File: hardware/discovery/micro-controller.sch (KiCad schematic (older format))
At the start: 3 parts, among them U4 STM32F407VG

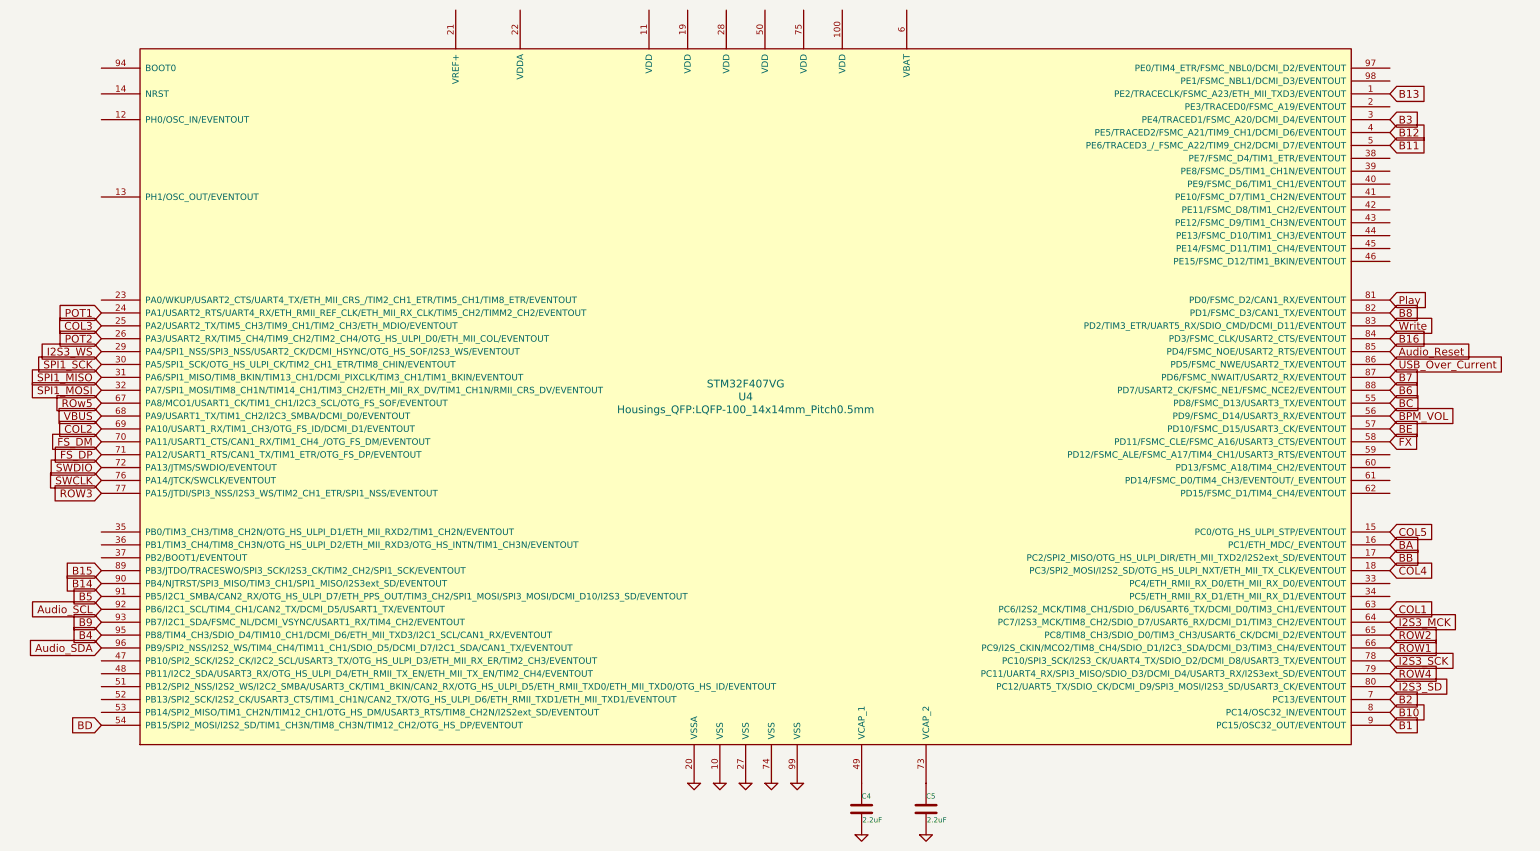
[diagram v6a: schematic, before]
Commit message: Discovery: Add audio DAC
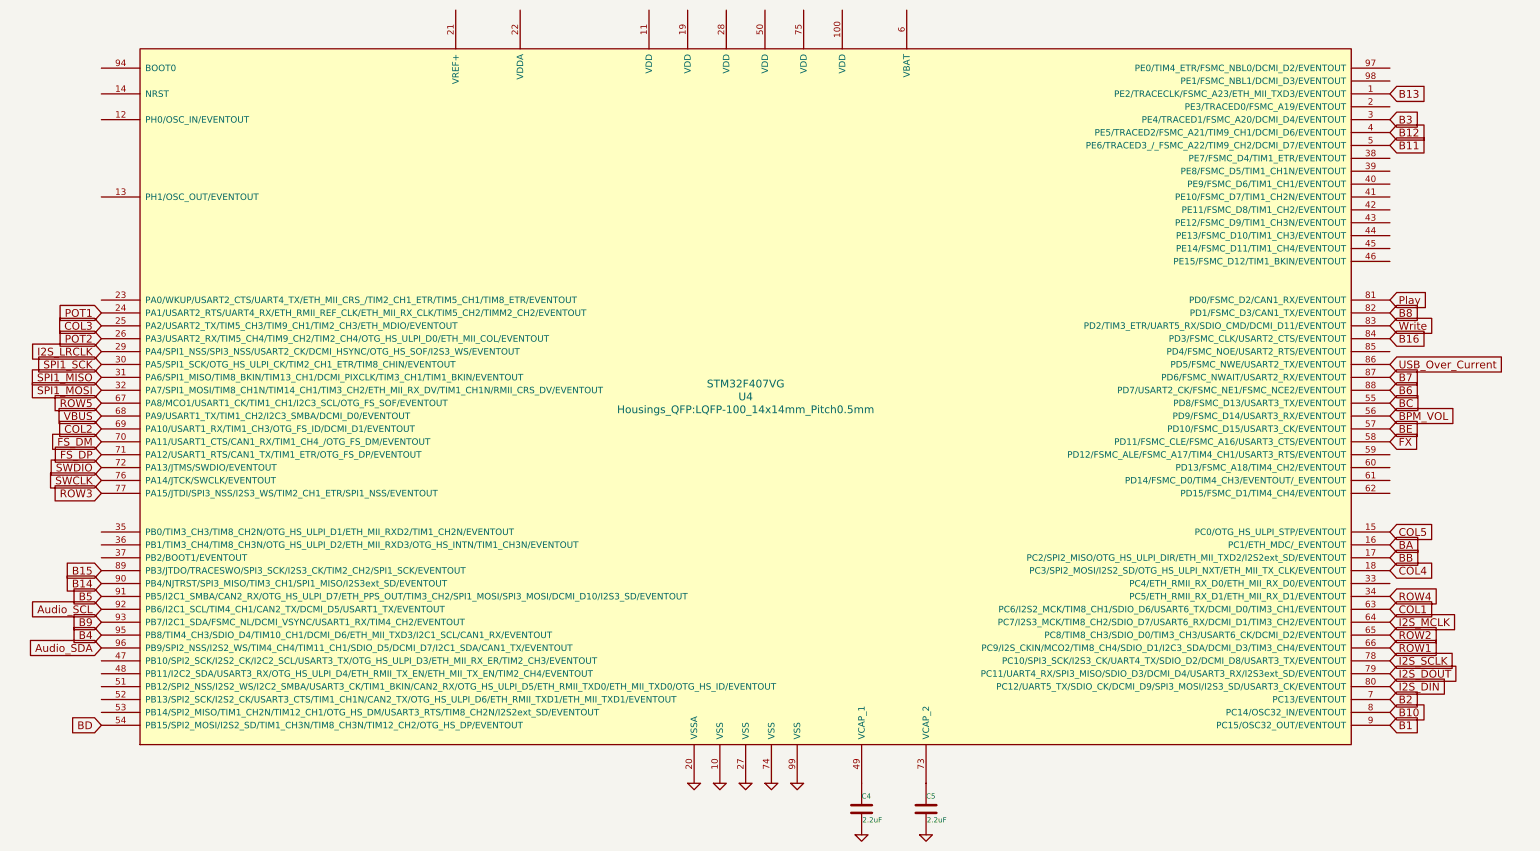
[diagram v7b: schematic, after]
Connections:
- net ROW4: now also U4.34 (PC5/ETH_RMII_RX_D1/ETH_MII_RX_D1/EVENTOUT); no longer U4.79 (PC11/UART4_RX/SPI3_MISO/SDIO_D3/DCMI_D4/USART3_RX/I2S3ext_SD/EVENTOUT)
- net Audio_Reset: no longer names the net of U4.85 (PD4/FSMC_NOE/USART2_RTS/EVENTOUT)
- net I2S3_MCK renamed I2S_MCLK
- net I2S3_SCK renamed I2S_SCLK
- net I2S3_SD renamed I2S_DIN
- net I2S3_WS renamed I2S_LRCLK
- net ROw5 renamed ROW5
- new net I2S_DOUT: U4.79 (PC11/UART4_RX/SPI3_MISO/SDIO_D3/DCMI_D4/USART3_RX/I2S3ext_SD/EVENTOUT)
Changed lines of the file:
@@
 POT2
 Text GLabel 2850 4500 0    60   Input ~ 0
-I2S3_WS
+I2S_LRCLK
 Text GLabel 2850 4600 0    60   Input ~ 0
 SPI1_SCK
@@
 SPI1_MOSI
 Text GLabel 2850 4900 0    60   Input ~ 0
-ROw5
+ROW5
 Text GLabel 2850 5000 0    60   Input ~ 0
 VBUS
@@
 COL1
 Text GLabel 12850 6600 2    60   Input ~ 0
-I2S3_MCK
+I2S_MCLK
 Text GLabel 12850 6700 2    60   Input ~ 0
 ROW2
@@
 ROW1
 Text GLabel 12850 6900 2    60   Input ~ 0
-I2S3_SCK
+I2S_SCLK
 Text GLabel 12850 7000 2    60   Input ~ 0
-ROW4
+I2S_DOUT
 Text GLabel 12850 7100 2    60   Input ~ 0
-I2S3_SD
+I2S_DIN
 Text GLabel 12850 7200 2    60   Input ~ 0
 B2
@@
 Text GLabel 12850 4400 2    60   Input ~ 0
 B16
-Text GLabel 12850 4500 2    60   Input ~ 0
-Audio_Reset
 Text GLabel 12850 4600 2    60   Input ~ 0
 USB_Over_Current
@@
 	1    0    0    -1
 $EndComp
+Text GLabel 12850 6400 2    60   Input ~ 0
+ROW4
 $EndSCHEMATC

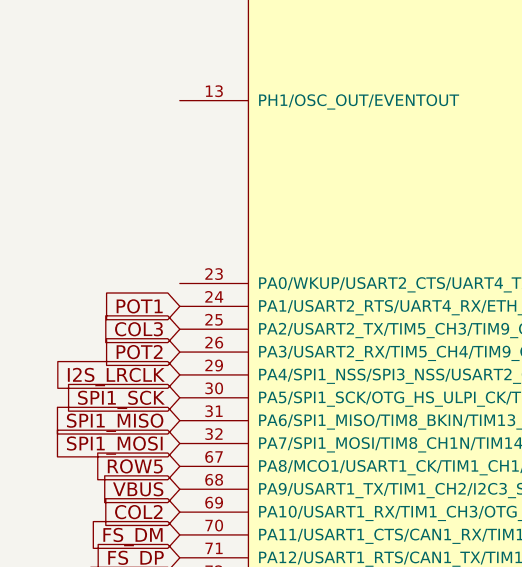
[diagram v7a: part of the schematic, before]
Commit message: Discovery: Connect all button to the wakeup pin
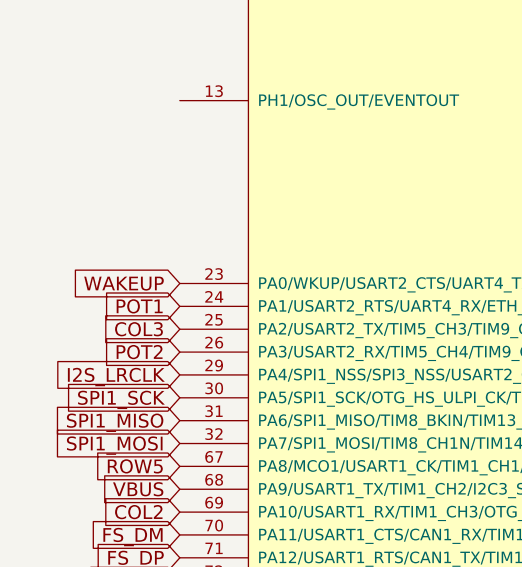
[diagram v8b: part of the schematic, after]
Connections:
- net WAKEUP: now reaches U4.23 (PA0/WKUP/USART2_CTS/UART4_TX/ETH_MII_CRS_/TIM2_CH1_ETR/TIM5_CH1/TIM8_ETR/EVENTOUT)
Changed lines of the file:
@@
 FS_DP
 $Comp
-L GND #PWR016
+L GND #PWR013
 U 1 1 585E3358
 P 7650 7850
-F 0 "#PWR016" H 7650 7850 30  0001 C CNN
+F 0 "#PWR013" H 7650 7850 30  0001 C CNN
 F 1 "GND" H 7650 7780 30  0001 C CNN
 F 2 "" H 7650 7850 60  0001 C CNN
@@
 $EndComp
 $Comp
-L GND #PWR017
+L GND #PWR014
 U 1 1 585E336D
 P 7850 7850
-F 0 "#PWR017" H 7850 7850 30  0001 C CNN
+F 0 "#PWR014" H 7850 7850 30  0001 C CNN
 F 1 "GND" H 7850 7780 30  0001 C CNN
 F 2 "" H 7850 7850 60  0001 C CNN
@@
 $EndComp
 $Comp
-L GND #PWR018
+L GND #PWR015
 U 1 1 585E337B
 P 8050 7850
-F 0 "#PWR018" H 8050 7850 30  0001 C CNN
+F 0 "#PWR015" H 8050 7850 30  0001 C CNN
 F 1 "GND" H 8050 7780 30  0001 C CNN
 F 2 "" H 8050 7850 60  0001 C CNN
@@
 $EndComp
 $Comp
-L GND #PWR019
+L GND #PWR016
 U 1 1 585E3389
 P 8250 7850
-F 0 "#PWR019" H 8250 7850 30  0001 C CNN
+F 0 "#PWR016" H 8250 7850 30  0001 C CNN
 F 1 "GND" H 8250 7780 30  0001 C CNN
 F 2 "" H 8250 7850 60  0001 C CNN
@@
 $EndComp
 $Comp
-L GND #PWR020
+L GND #PWR017
 U 1 1 585E3397
 P 7450 7850
-F 0 "#PWR020" H 7450 7850 30  0001 C CNN
+F 0 "#PWR017" H 7450 7850 30  0001 C CNN
 F 1 "GND" H 7450 7780 30  0001 C CNN
 F 2 "" H 7450 7850 60  0001 C CNN
@@
 $EndComp
 $Comp
-L GND #PWR021
+L GND #PWR018
 U 1 1 585E35DF
 P 8750 8250
-F 0 "#PWR021" H 8750 8250 30  0001 C CNN
+F 0 "#PWR018" H 8750 8250 30  0001 C CNN
 F 1 "GND" H 8750 8180 30  0001 C CNN
 F 2 "" H 8750 8250 60  0001 C CNN
@@
 $EndComp
 $Comp
-L GND #PWR022
+L GND #PWR019
 U 1 1 585E35F3
 P 9250 8250
-F 0 "#PWR022" H 9250 8250 30  0001 C CNN
+F 0 "#PWR019" H 9250 8250 30  0001 C CNN
 F 1 "GND" H 9250 8180 30  0001 C CNN
 F 2 "" H 9250 8250 60  0001 C CNN
@@
 Text GLabel 12850 6400 2    60   Input ~ 0
 ROW4
+Text GLabel 2850 4100 0    60   Input ~ 0
+WAKEUP
 $EndSCHEMATC
